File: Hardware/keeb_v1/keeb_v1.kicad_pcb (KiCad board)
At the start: 2 copper layers, 25 parts, among them J1 USB_mini_micro_B, K1 KEYSW, K2 KEYSW, K3 KEYSW, K4 KEYSW, SW1 SW_Push, U1 ATMEGA32U4, X1 XTAL_GND

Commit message: Psych, this is the first commit!
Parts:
- K1, K2, K3, K4: moved to F.Cu
- moved D4 79.2 mm to (105.4, 128.3)
- moved C6 65.9 mm to (119.4, 153.7)
- moved C8 60.5 mm to (124.5, 148.6)
- moved C9 60.5 mm to (124.5, 153.7)
- moved C7 59.5 mm to (124.5, 137.2)
- moved C5 56.2 mm to (119.4, 139.7)
- moved C4 55.0 mm to (119.4, 144.8)
- moved C3 54.3 mm to (119.4, 148.6)
- moved D1 49.6 mm to (86.4, 109.2)
- moved C2 47.6 mm to (124.5, 143.5)
- moved D3 44.4 mm to (86.4, 128.3)
- moved D2 41.5 mm to (105.4, 109.2)
- moved SW1 38.1 mm to (141.0, 119.4)
- moved J1 33.0 mm to (129.5, 120.7)
- moved X1 26.2 mm to (146.1, 110.5)
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
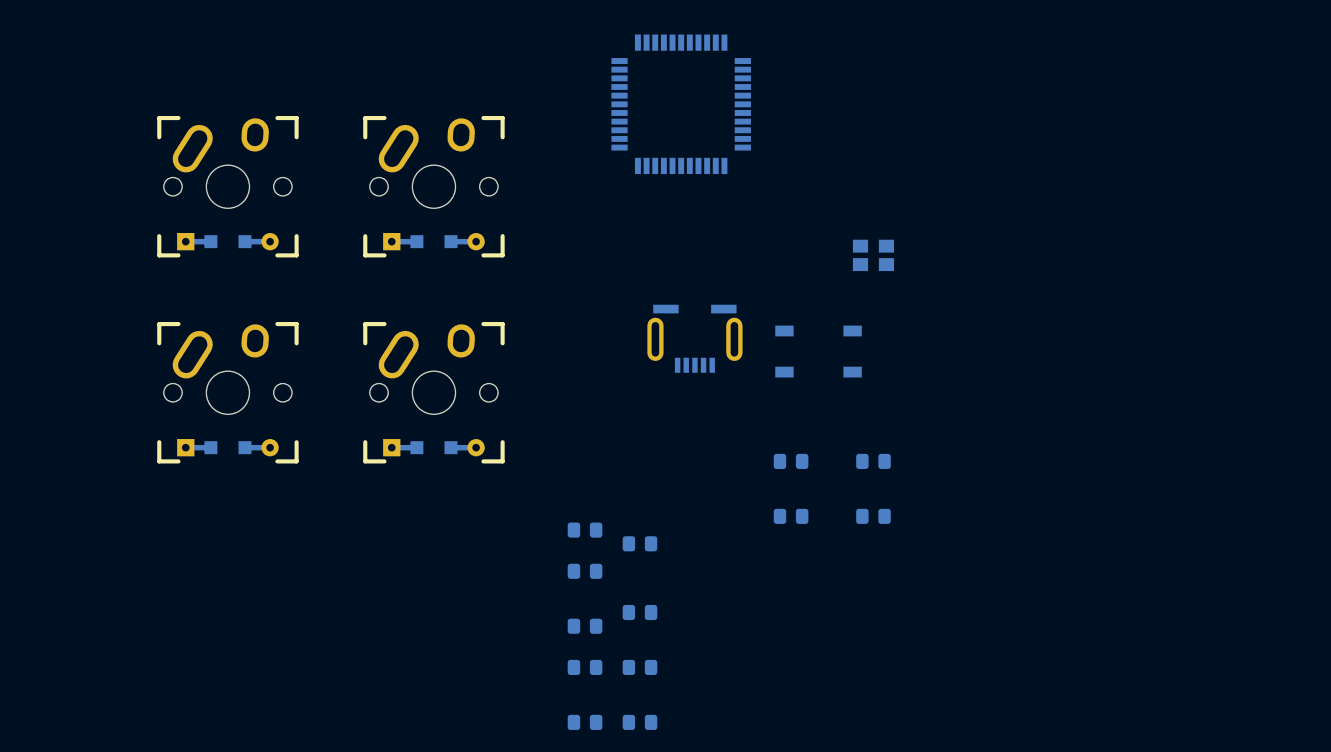
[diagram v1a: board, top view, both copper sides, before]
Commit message: Started routing. Need to go back and check lengths and also add mounting holes
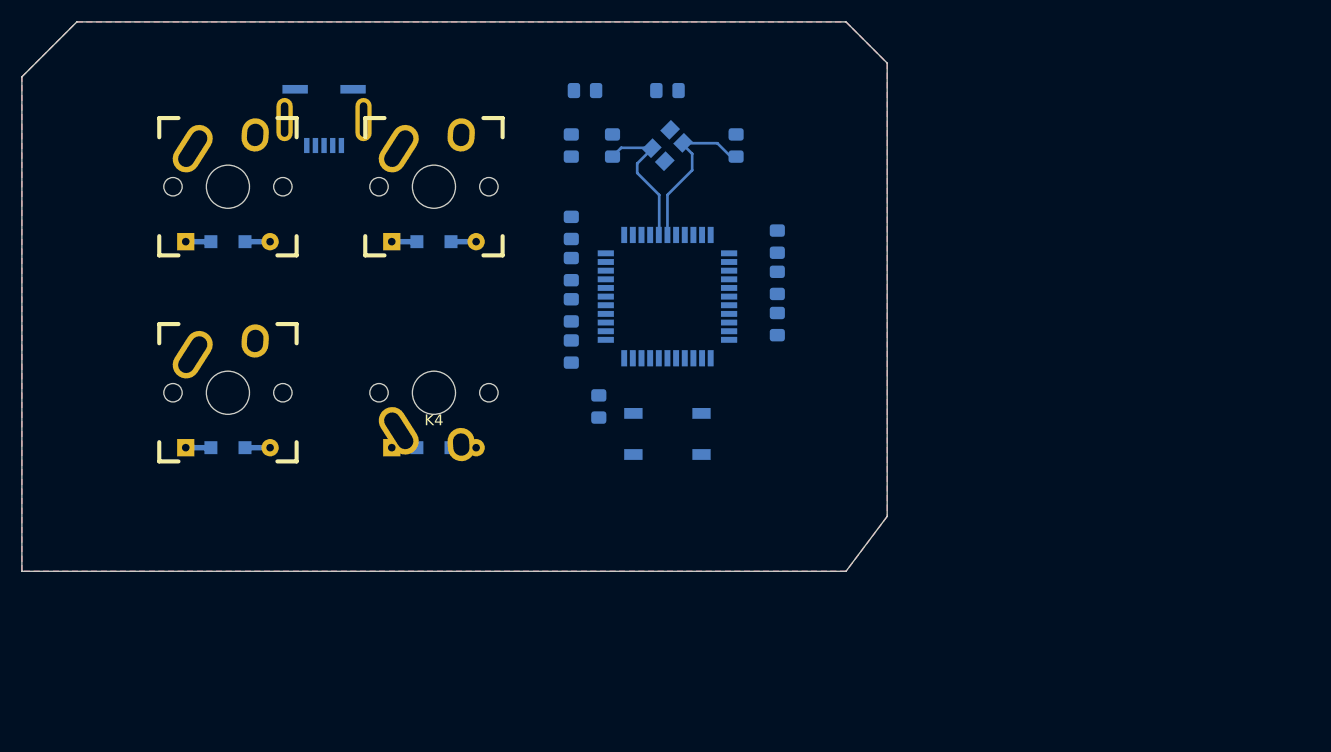
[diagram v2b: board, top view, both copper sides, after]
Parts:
- K4: moved to B.Cu
- moved C6 53.4 mm to (118.1, 100.3), turned to 90 degrees
- moved C9 46.2 mm to (118.1, 108.0), turned to 90 degrees
- moved C2 44.1 mm to (133.3, 100.3), turned to 90 degrees
- moved R3 43.7 mm to (127.0, 95.2), turned to 180 degrees
- moved R4 43.7 mm to (119.4, 95.2), turned to 180 degrees
- moved J1 39.9 mm to (95.2, 100.3)
- moved C4 39.8 mm to (137.2, 109.2), turned to 270 degrees
- moved C3 36.4 mm to (137.2, 116.8), turned to 270 degrees
- moved C1 35.7 mm to (121.9, 100.3), turned to 90 degrees
- moved C8 29.9 mm to (118.1, 119.4), turned to 90 degrees
- moved C5 28.0 mm to (118.1, 111.8), turned to 90 degrees
- moved D2 26.9 mm to (86.4, 128.3)
- moved D3 26.9 mm to (105.4, 109.2)
- moved K1 26.9 mm to (86.4, 104.1)
- moved K2 26.9 mm to (86.4, 123.2)
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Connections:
- net +5V renamed GND
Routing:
- net Net-(C2-Pad1): track 0.00 -> 15.3 mm
- net Net-(C1-Pad1): track 0.00 -> 13.6 mm
- added copper zone on B.Cu, net GND
- added copper zone on F.Cu, net GND
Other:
- board outline added: 80 x 50.8 mm

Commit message: Done routing and it's ugly
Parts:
- K4: moved to F.Cu
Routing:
- net VCC: track 0.00 -> 119.0 mm, vias 0 -> 2
- net /col0: track 0.00 -> 73.6 mm, vias 0 -> 2
- net /col1: track 0.00 -> 63.7 mm, vias 0 -> 2
- net Net-(J1-Pad2): track 0.00 -> 63.0 mm, vias 0 -> 2
- net /row0: track 0.00 -> 56.5 mm, vias 0 -> 4
- net Net-(J1-Pad3): track 0.00 -> 51.4 mm
- net /row1: track 0.00 -> 51.0 mm, vias 0 -> 2
- net GND: track 0.00 -> 47.9 mm, vias 0 -> 8
- net Net-(R3-Pad1): track 0.00 -> 33.2 mm, vias 0 -> 2
- net Net-(R1-Pad1): track 0.00 -> 29.4 mm, vias 0 -> 2
- net Net-(R4-Pad1): track 0.00 -> 24.8 mm, vias 0 -> 2
- net Net-(D2-Pad2): track 0.00 -> 10.4 mm
- net Net-(D1-Pad2): track 0.00 -> 10.4 mm
- net Net-(D4-Pad2): track 0.00 -> 10.4 mm
- net Net-(D3-Pad2): track 0.00 -> 10.4 mm
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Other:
- board text added: "keebsie"
